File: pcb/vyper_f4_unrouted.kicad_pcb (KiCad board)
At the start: 4 copper layers, 30 x 64 mm, 81 parts, among them J1 USB_SERVICE_SH1.0_4P, J2 ESC_SH1.0_8P, J3 RX_UART1, J4 GPS_UART3, J5 EXTERNAL_I2C, J6 VTX_UART6, J7 SWD, J8 BEEPER_PAD, U1 STM32F405RGTx, U2 ICM-42688-P, U3 TPS54360DDA, U4 AP2112K-3.3, U5 AP2112K-3.3, U6 W25Q128JVS, U7 BMP280, U8 SN74AHCT1G125DBVR, Y1 8MHz 10pF

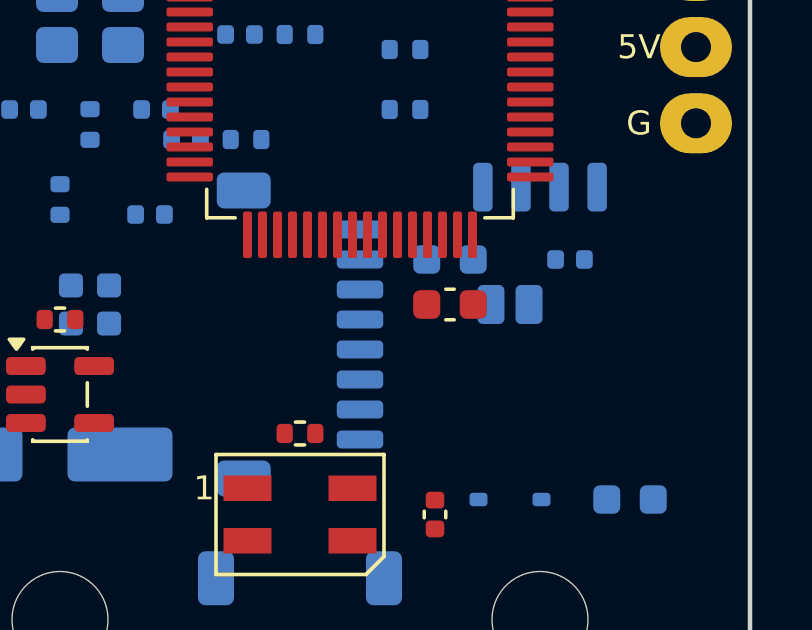
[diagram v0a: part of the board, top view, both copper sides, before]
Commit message: Route STM32 VCAP regulator networks
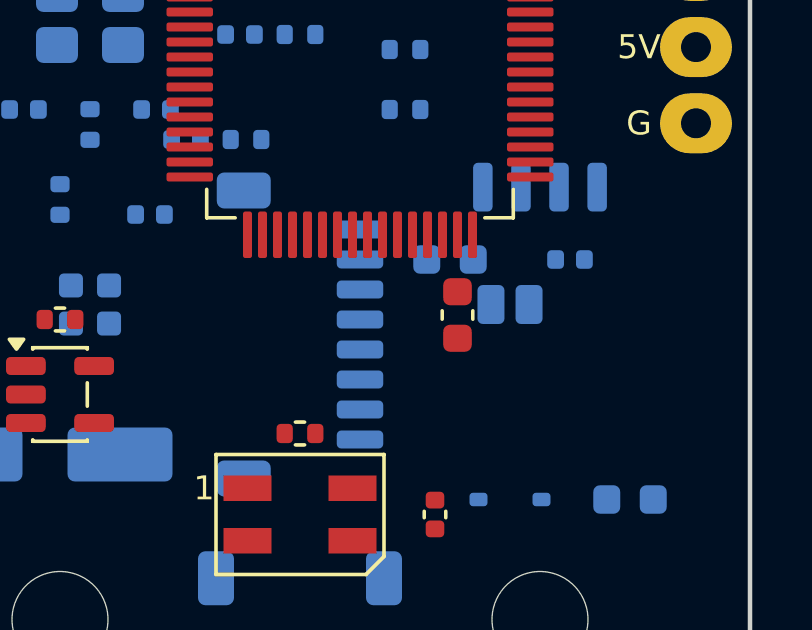
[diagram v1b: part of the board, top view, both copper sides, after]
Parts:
- moved C19 0.43 mm to (5.25, 17.9), turned to -90 degrees

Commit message: Route Vyper FC logic and analog supply planes
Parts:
- C12, C13: moved to F.Cu
- moved FB1 9.75 mm to (-5.80, 11.8), turned to 90 degrees
- moved C12 9.70 mm to (-7.40, 10.7), turned to 180 degrees
- moved C13 9.15 mm to (-7.40, 12.0), turned to 180 degrees

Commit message: Complete Vyper FC MCU power fanout
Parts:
- U6: value W25Q128JVS -> W25Q128JVPIM; footprint SOIC-8_5.3x5.3mm_P1.27mm -> WDFN-8-1EP_6x5mm_P1.27mm_EP3.4x4mm
- moved C18 5.10 mm to (10.0, 15.0)
- moved C16 5.00 mm to (4.30, 14.3), turned to 180 degrees
- moved C14 3.44 mm to (-2.80, 5.00), turned to 180 degrees
- moved C15 2.04 mm to (6.20, 5.75), turned to 180 degrees

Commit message: Specify exact FC USB protection
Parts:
- removed D5, D6: PESD5V low-C, D_SOD-323
- added U9: USBLC6-2SC6, SOT-666, F.Cu at (0.00, 21.5)
- R14, R15: moved to F.Cu
- moved R15 21.7 mm to (10.6, 8.30)
- moved R14 18.2 mm to (9.30, 8.30)
- moved C31 11.5 mm to (-7.00, 24.5)
- moved R19 4.55 mm to (-4.50, 22.5)
- moved D4 2.50 mm to (-2.00, 26.0)
- moved C28 0.50 mm to (10.5, 24.0), turned to 90 degrees
- turned D7 to 180 degrees

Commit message: Route and match Vyper FC USB
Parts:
- R14, R15: value 22R -> ERJ2RKF22R0X 22R 1%
- moved D4 2.24 mm to (0.00, 27.0)
- moved R14 0.99 mm to (10.0, 9.00), turned to 180 degrees
- moved C20 0.95 mm to (9.85, 5.47), turned to 90 degrees
- moved R15 0.78 mm to (10.0, 7.80), turned to 180 degrees
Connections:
- J1 pad 3: USB_DM_RAW -> USB_DP_RAW
- J1 pad 4: USB_DP_RAW -> USB_DM_RAW
